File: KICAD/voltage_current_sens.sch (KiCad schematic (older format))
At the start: 26 parts

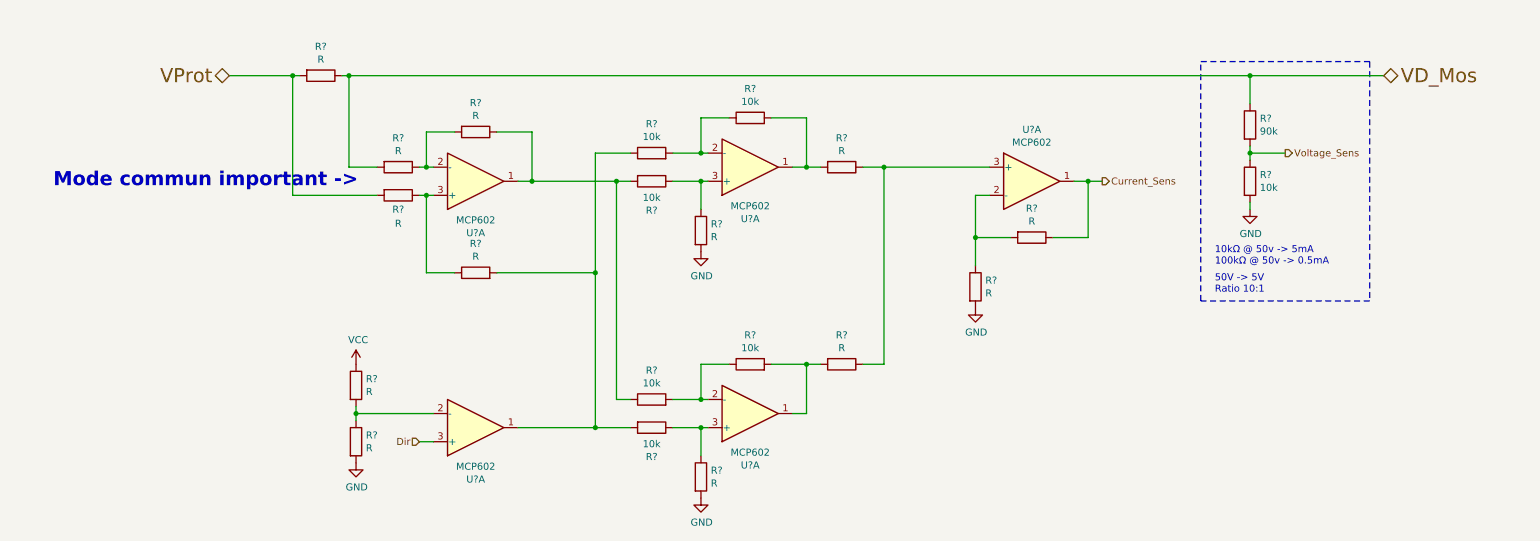
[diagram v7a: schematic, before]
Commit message: minors edits + 7v rail
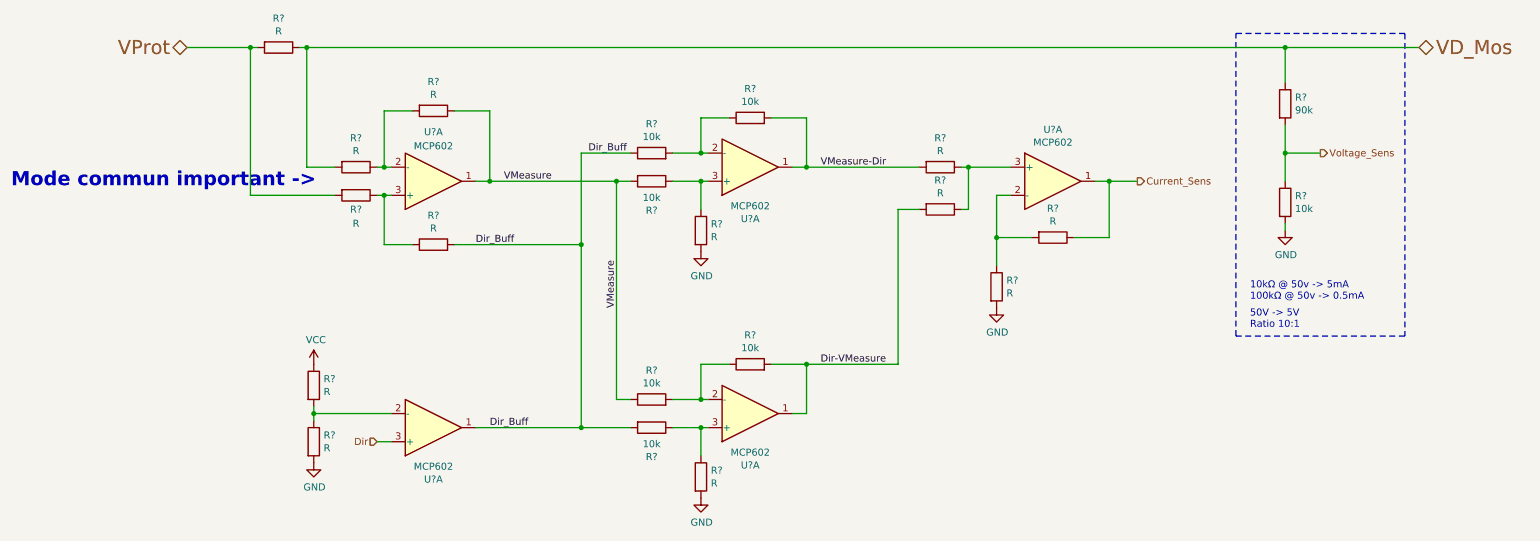
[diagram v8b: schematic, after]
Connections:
- net VMeasure: now reaches R?.1, R?.1, R?.2, U?.1
- net Dir_Buff: now reaches R?.1, R?.2, R?.2, U?.1
- net Dir-VMeasure: now reaches R?.2, R?.2, U?.1
- net VMeasure-Dir: now reaches R?.2, R?.2, U?.1
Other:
- moved on the sheet: R?, U?A
